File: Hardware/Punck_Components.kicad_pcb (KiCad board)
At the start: 4 copper layers, 91.2 x 99.8 mm, 112 parts, among them J1 Conn_01x12_Female, J2 Conn_01x12_Female, J3 Conn_01x12_Female, J4 Conn_01x12_Female, J5 SWD_Header, J6 Eurorack_10_pin_power, Q1 MMBT3904, Q2 MMBT3904, Q3 MMBT3904, Q4 MMBT3904, Q5 MMBT3904, Q6 MMBT3904, Q7 MMBT3904, U1 TL074, U2 STM32H743ZITx, U3 W25Q128JVS, U4 PCM5100APW, U5 TPS561201, U6 W25Q128JVS, U7 LD1117-3.3-4Tab, Y1 8MHz 20pF

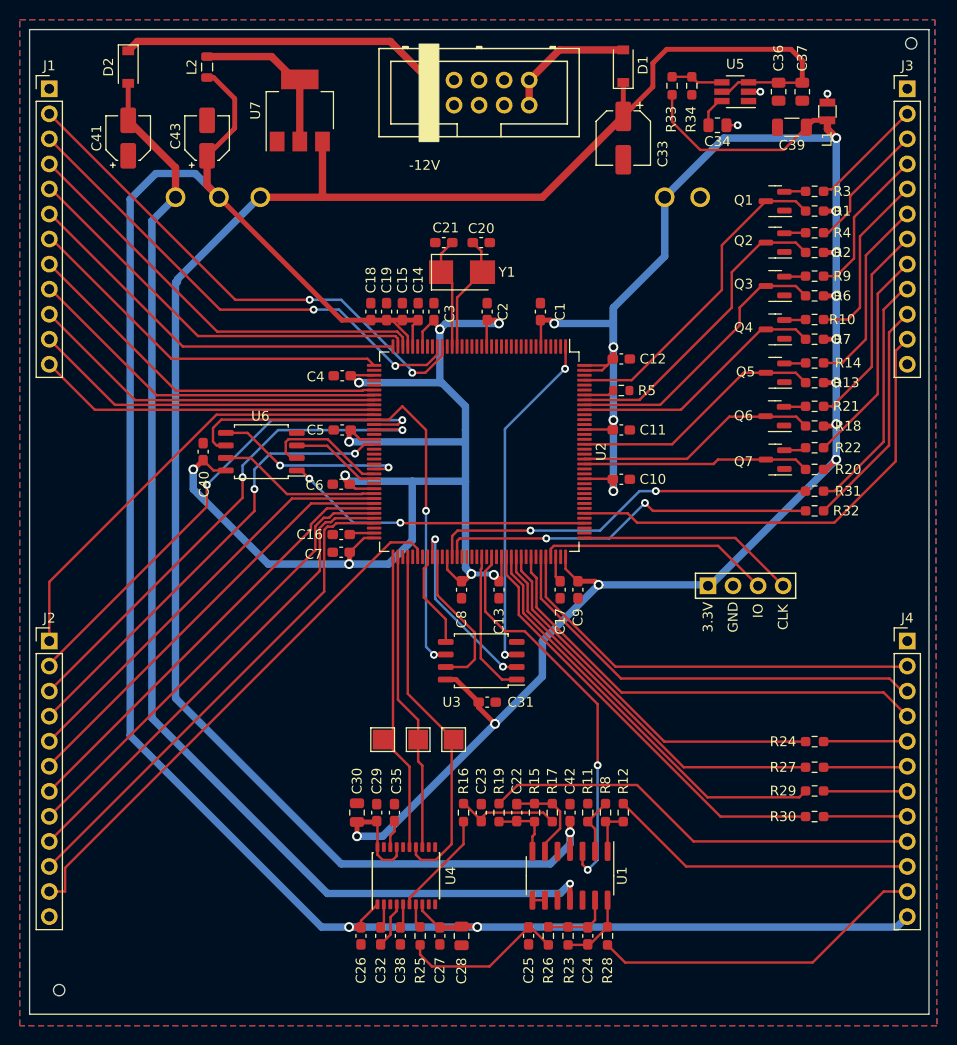
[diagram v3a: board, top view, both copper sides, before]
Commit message: Component PCB first draft
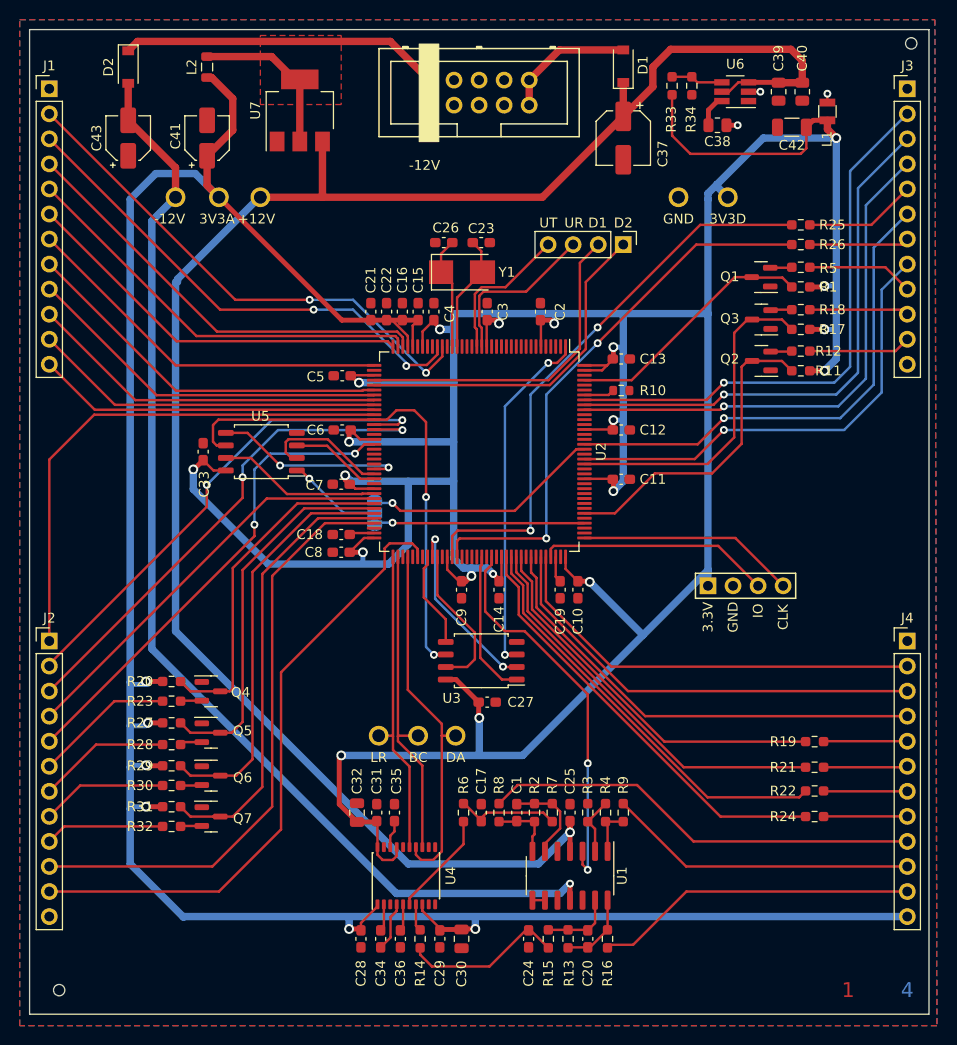
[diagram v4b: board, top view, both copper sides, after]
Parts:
- added FID1: 4_Layer_Marker, Custom_Footprints:4_Layer_Markers, F.Cu at (156.0, 147.4)
- added J5: Debug_Header, Connector_PinHeader_2.54mm:PinHeader_1x04_P2.54mm_Vertical, F.Cu at (130.2, 71.8)
- added JP1: QSPI2_NCS_Select, Jumper:SolderJumper-3_P1.3mm_Bridged12_RoundedPad1.0x1.5mm, B.Cu at (105.0, 99.0)
- C17: renamed from C23; value 1nF -> 2n2
- C24: renamed from C25; value 1nF -> 2n2
- R14: renamed from R25; value 2k2 -> 1k
- R15: renamed from R26; value 10k -> 15k
- R6: renamed from R16; value 2k2 -> 1k
- R7: renamed from R17; value 10k -> 15k
- TP1: renamed from TP6; footprint TestPoint:TestPoint_Pad_2.0x2.0mm -> Custom_Footprints:1.3mm_Test_Point
- TP2: renamed from TP7; footprint TestPoint:TestPoint_Pad_2.0x2.0mm -> Custom_Footprints:1.3mm_Test_Point
- TP3: renamed from TP8; footprint TestPoint:TestPoint_Pad_2.0x2.0mm -> Custom_Footprints:1.3mm_Test_Point
- moved R30 86.0 mm to (84.4, 126.7), turned to 0 degrees
- moved R29 83.4 mm to (84.4, 124.7), turned to 180 degrees
- moved R32 83.0 mm to (84.4, 130.8), turned to 0 degrees
- moved R31 80.6 mm to (84.4, 128.8), turned to 180 degrees
- moved Q6 78.7 mm to (88.4, 125.7), turned to 0 degrees
- moved Q7 75.6 mm to (88.4, 129.8), turned to 0 degrees
- moved R23 73.7 mm to (84.4, 118.1), turned to 0 degrees
- moved R20 71.9 mm to (84.4, 116.1), turned to 180 degrees
- moved R28 71.8 mm to (84.4, 122.5), turned to 0 degrees
- moved R27 70.1 mm to (84.4, 120.3), turned to 180 degrees
- moved Q4 65.7 mm to (88.4, 117.1), turned to 0 degrees
- moved Q5 63.6 mm to (88.4, 121.3), turned to 0 degrees
- moved R25 27.0 mm to (148.2, 69.8)
- moved R26 27.0 mm to (148.2, 71.8)
- moved Q1 14.2 mm to (144.2, 75.1)
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- renumbered C22 to C1, C9 to C10, C10 to C11, C11 to C12, C12 to C13, C13 to C14, C14 to C15, C15 to C16, C16 to C18, C17 to C19, C1 to C2, C24 to C20, C18 to C21, C19 to C22, C20 to C23, C42 to C25, C21 to C26, C31 to C27, C26 to C28, C27 to C29, C2 to C3, C28 to C30, C29 to C31, C30 to C32, C40 to C33, C32 to C34, C38 to C36, C33 to C37, C34 to C38, C36 to C39, C3 to C4, C37 to C40, C43 to C41, C39 to C42, C41 to C43, C4 to C5, C5 to C6, C6 to C7, C7 to C8, C8 to C9, J5 to J6, J6 to J7, Q6 to Q1, Q3 to Q2, Q1 to Q3, Q5 to Q4, Q7 to Q5, Q2 to Q6, Q4 to Q7, R18 to R1, R5 to R10, R6 to R11, R9 to R12, R23 to R13, R28 to R16, R1 to R17, R3 to R18, R24 to R19, R15 to R2, R13 to R20, R27 to R21, R29 to R22, R14 to R23, R30 to R24, R31 to R25, R32 to R26, R20 to R27, R22 to R28, R2 to R29, R11 to R3, R4 to R30, R7 to R31, R10 to R32, R8 to R4, R21 to R5, R19 to R8, R12 to R9, TP1 to TP4, TP2 to TP5, TP3 to TP6, TP4 to TP7, TP5 to TP8, U6 to U5, U5 to U6
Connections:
- J1 pad 10: /SAMPLER_A_VOL_POT -> /SNARE_VOL_POT
- J1 pad 11: /SAMPLER_B_VOICE_POT -> /SAMPLER_A_SPEED_POT
- J1 pad 12: /HIHAT_DECAY_POT -> /SAMPLER_B_VOICE_POT
- J1 pad 2: /SAMPLER_A_VOICE_POT -> /SNARE_FILTER_POT
- J1 pad 3: /SAMPLER_A_SPEED_POT -> /SAMPLER_A_VOICE_POT
- J1 pad 7: /SNARE_FILTER_POT -> /SNARE_TUNING_POT
- J1 pad 8: /SNARE_TUNING_POT -> /HIHAT_DECAY_POT
- J1 pad 9: /SNARE_VOL_POT -> /SAMPLER_B_SPEED_POT
- J2 pad 10: /CH_BTN -> /MIDI_LEARN
- J2 pad 11: /KI_BTN -> /SEQ_SELECT
- J2 pad 2: /SAMPLER_B_SPEED_POT -> /SAMPLER_A_VOL_POT
- J2 pad 4: /TEMPO_POT -> /CH_BTN
- J2 pad 5: /MIDI_LEARN -> /TEMPO_POT
- J2 pad 6: /SEQ_SELECT -> /CH_IN
- J2 pad 7: /SA_BTN -> /OH_IN
- J2 pad 8: /SB_BTN -> /SAMPLER_A_IN
- J2 pad 9: /SN_BTN -> /SAMPLER_B_IN
- J3 pad 10: /SB_LED -> /SNARE_IN
- J3 pad 11: /OH_BTN -> /KICK_IN
- J3 pad 12: unconnected-(J3-Pad12) -> GND
- J3 pad 2: /KICK_IN -> /SA_BTN
- J3 pad 3: /SAMPLER_A_IN -> /KI_BTN
- J3 pad 4: /SNARE_IN -> /SN_BTN
- J3 pad 5: /SAMPLER_B_IN -> /SA_LED
- J3 pad 6: /CH_IN -> /SB_BTN
- J3 pad 7: /MIDI_IN -> /SB_LED
- J3 pad 8: /OH_IN -> /OH_BTN
- J3 pad 9: /SA_LED -> /MIDI_IN
- Q1 pad 3: /MIDI_CLAMP -> /MIDI_UART
- Q2 pad 3: /SNARE_CLAMP -> /KICK_CLAMP
- Q3 pad 3: /KICK_CLAMP -> /SNARE_CLAMP
- R1 pad 1: /MIDI_CLAMP -> /MIDI_UART
- R11 pad 1: /SNARE_CLAMP -> /KICK_CLAMP
- R12 pad 1: /SNARE_IN -> /KICK_IN
- R17 pad 1: /KICK_CLAMP -> /SNARE_CLAMP
- R18 pad 1: /KICK_IN -> /SNARE_IN
- R20 pad 2: +3V3 -> +3.3VA
- R27 pad 2: +3V3 -> +3.3VA
- R29 pad 2: +3V3 -> +3.3VA
- R31 pad 2: +3V3 -> +3.3VA
- U2 pad 114: /OH_BTN -> /KICK_CLAMP
- U2 pad 124: /OH_CLAMP -> /SNARE_CLAMP
- U2 pad 125: /MIDI_CLAMP -> /OH_BTN
- U2 pad 127: unconnected-(U2-Pad127) -> /OCTOSPIM_P2_NCS
- U2 pad 128: /CH_CLAMP -> /SB_BTN
- U2 pad 135: /SAMPLER_B_CLAMP -> /SN_BTN
- U2 pad 136: /SNARE_CLAMP -> /KI_BTN
- U2 pad 137: /SAMPLER_A_CLAMP -> /SA_BTN
- U2 pad 141: /KICK_CLAMP -> /MIDI_UART
- U2 pad 18: unconnected-(U2-Pad18) -> /UART_RX
- U2 pad 19: unconnected-(U2-Pad19) -> /UART_TX
- U2 pad 26: /SAMPLER_A_VOICE_POT -> /SNARE_FILTER_POT
- U2 pad 27: /SAMPLER_A_SPEED_POT -> /SAMPLER_A_VOICE_POT
- U2 pad 37: /SNARE_FILTER_POT -> /SNARE_TUNING_POT
- U2 pad 42: /SNARE_TUNING_POT -> /HIHAT_DECAY_POT
- U2 pad 43: /SNARE_VOL_POT -> /SAMPLER_B_SPEED_POT
- U2 pad 44: /SAMPLER_A_VOL_POT -> /SNARE_VOL_POT
- U2 pad 45: /SAMPLER_B_VOICE_POT -> /SAMPLER_A_SPEED_POT
- U2 pad 46: /HIHAT_DECAY_POT -> /SAMPLER_B_VOICE_POT
- U2 pad 49: /SAMPLER_B_SPEED_POT -> /SAMPLER_A_VOL_POT
- U2 pad 64: /MIDI_LEARN -> /CH_BTN
- U2 pad 65: /SEQ_SELECT -> /CH_CLAMP
- U2 pad 66: /SA_BTN -> /OH_CLAMP
- U2 pad 67: /SB_BTN -> /SAMPLER_A_CLAMP
- U2 pad 68: /SN_BTN -> /SAMPLER_B_CLAMP
- U2 pad 69: /CH_BTN -> /MIDI_LEARN
- U2 pad 78: /KI_BTN -> /SEQ_SELECT
- U5 pad 1: /QSPI_BK2_NCS -> Net-(JP1-Pad2)
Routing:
- net /DAC2: track 0.00 -> 35.1 mm
- net /DAC1: track 0.00 -> 33.5 mm
- net /MIDI_UART: track 0.00 -> 25.8 mm
- net /MIDI_CLAMP: track 24.6 -> 0.00 mm
- net +3V3: track 373.7 -> 398.1 mm, vias 24 -> 20
- net /OCTOSPIM_P2_NCS: track 0.00 -> 24.3 mm, vias 0 -> 1
- net +3.3VA: track 210.9 -> 233.4 mm, vias 2 -> 6
- net /SAMPLER_B_CLAMP: track 26.2 -> 46.4 mm
- net /SEQ_SELECT: track 44.0 -> 63.6 mm
- net /MIDI_LEARN: track 43.1 -> 61.1 mm
- net /SA_LED_OUT: track 39.8 -> 57.7 mm
- net /SB_LED_OUT: track 38.9 -> 56.5 mm
- net /UART_RX: track 0.00 -> 16.9 mm
- net /OH_CLAMP: track 23.0 -> 38.5 mm
- net /UART_TX: track 0.00 -> 14.9 mm
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- added copper zone on F.Cu, net /VO
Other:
- board text added: "+12V"
- board text added: "-12V"
- board text added: "3V3A"
- board text added: "3V3D"
- board text added: "BC"
- board text added: "D1"
- board text added: "D2"
- board text added: "DA"
- board text added: "GND"
- board text added: "H723"
- board text added: "H743"
- board text added: "LR"
- board text added: "UR"
- board text added: "UT"

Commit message: Started panel layout
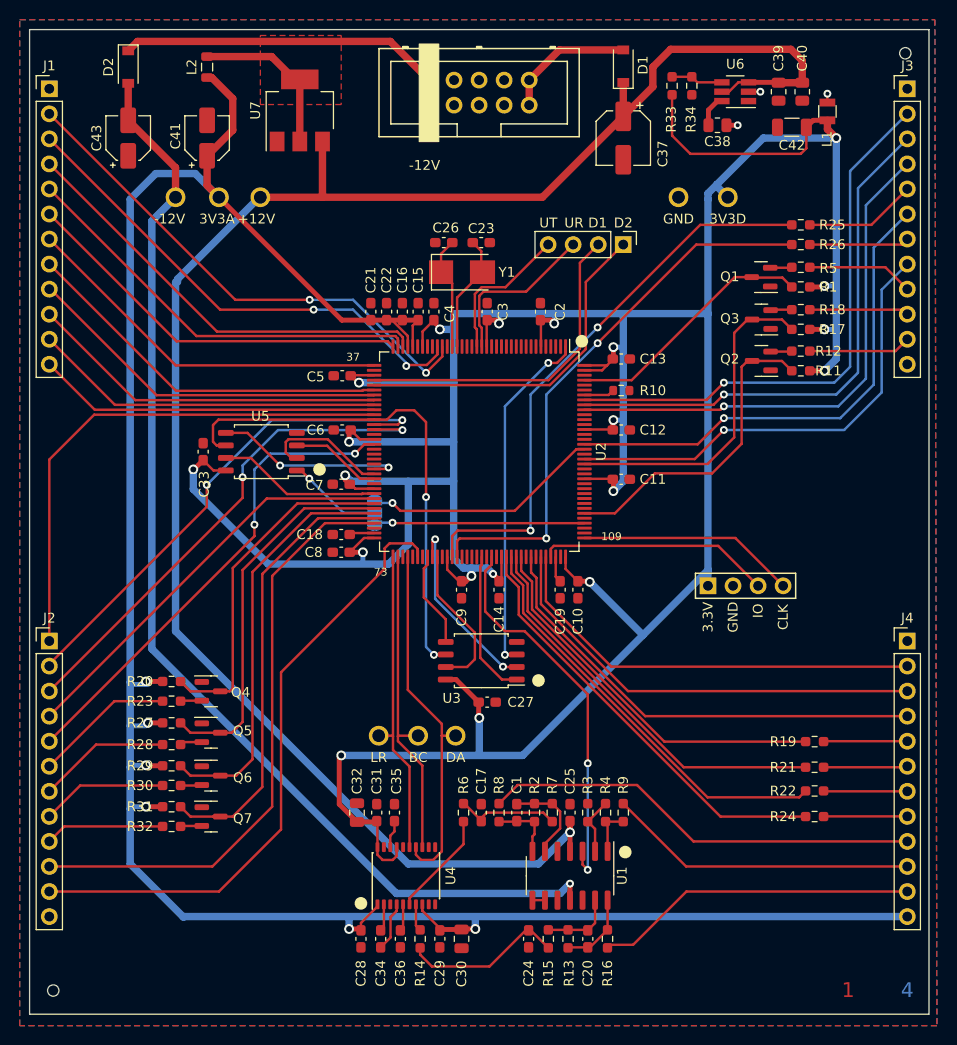
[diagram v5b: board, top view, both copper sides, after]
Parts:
- moved H2 1.17 mm to (158.8, 52.4)
- moved H1 0.60 mm to (72.4, 147.4)
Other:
- board text added: "109"
- board text added: "37"
- board text added: "73"
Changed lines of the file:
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@@
   )
   (footprint "Custom_Footprints:JLC_SMT_Tooling_Hole" (layer "F.Cu")
-    (at 73 147.4)
+    (at 72.4 147.44)
     (descr "Mounting Hole 2.2mm, no annular, M2")
     (tags "mounting hole 2.2mm no annular m2")
@@
   )
   (footprint "Custom_Footprints:JLC_SMT_Tooling_Hole" (layer "F.Cu")
-    (at 159.4 51.4)
+    (at 158.8 52.4)
     (descr "Mounting Hole 2.2mm, no annular, M2")
     (tags "mounting hole 2.2mm no annular m2")
@@
       ))
   )
+  (gr_circle (center 126 81.6) (end 126.565685 81.6) (layer "F.SilkS") (width 0.15) (fill solid))
+  (gr_circle (center 130.4 133.4) (end 130.965685 133.4) (layer "F.SilkS") (width 0.15) (fill solid))
+  (gr_circle (center 121.6 116) (end 122.165685 116) (layer "F.SilkS") (width 0.15) (fill solid))
+  (gr_circle (center 99.4 94.6) (end 99.965685 94.6) (layer "F.SilkS") (width 0.15) (fill solid))
+  (gr_circle (center 103.6 138.6) (end 104.165685 138.6) (layer "F.SilkS") (width 0.15) (fill solid))
   (gr_rect (start 93.4 52) (end 101.6 57.665779) (layer "F.Mask") (width 0.15) (fill solid))
   (gr_line locked (start 115.6 48) (end 115.6 153) (layer "Dwgs.User") (width 0.15))
@@
     (effects (font (size 1 1) (thickness 0.15)) (justify mirror))
   )
+  (gr_text "73" (at 105.6 105) (layer "F.SilkS")
+    (effects (font (size 0.8 0.8) (thickness 0.12)))
+  )
   (gr_text "DA" (at 113.2 123.8) (layer "F.SilkS")
     (effects (font (size 1 1) (thickness 0.15)))
@@
     (effects (font (size 1 1) (thickness 0.15)))
   )
+  (gr_text "37" (at 102.8 83.2) (layer "F.SilkS")
+    (effects (font (size 0.8 0.8) (thickness 0.12)))
+  )
   (gr_text "D1" (at 127.6 69.6) (layer "F.SilkS")
     (effects (font (size 1 1) (thickness 0.15)))
   )
+  (gr_text "109" (at 129 101.4) (layer "F.SilkS")
+    (effects (font (size 0.8 0.8) (thickness 0.12)))
+  )
   (gr_text "UT" (at 122.6 69.6) (layer "F.SilkS")

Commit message: Updated components on panel board
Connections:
- J1 pad 12: /SAMPLER_B_VOICE_POT -> /SAMPLER_B_SPEED_POT
- J1 pad 9: /SAMPLER_B_SPEED_POT -> /SAMPLER_B_VOICE_POT
- U2 pad 43: /SAMPLER_B_SPEED_POT -> /SAMPLER_B_VOICE_POT
- U2 pad 46: /SAMPLER_B_VOICE_POT -> /SAMPLER_B_SPEED_POT
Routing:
- net /SAMPLER_B_VOICE_POT: track 34.8 -> 37.4 mm
- net /SAMPLER_B_SPEED_POT: track 37.4 -> 34.8 mm
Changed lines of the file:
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@@
       (net 25 "/HIHAT_DECAY_POT") (pinfunction "Pin_8") (pintype "passive"))
     (pad "9" thru_hole oval (at 0 20.32) (size 1.7 1.7) (drill 1) (layers *.Cu *.Mask)
-      (net 31 "/SAMPLER_B_SPEED_POT") (pinfunction "Pin_9") (pintype "passive"))
+      (net 30 "/SAMPLER_B_VOICE_POT") (pinfunction "Pin_9") (pintype "passive"))
     (pad "10" thru_hole oval (at 0 22.86) (size 1.7 1.7) (drill 1) (layers *.Cu *.Mask)
       (net 23 "/SNARE_VOL_POT") (pinfunction "Pin_10") (pintype "passive"))
@@
       (net 28 "/SAMPLER_A_SPEED_POT") (pinfunction "Pin_11") (pintype "passive"))
     (pad "12" thru_hole oval (at 0 27.94) (size 1.7 1.7) (drill 1) (layers *.Cu *.Mask)
-      (net 30 "/SAMPLER_B_VOICE_POT") (pinfunction "Pin_12") (pintype "passive"))
+      (net 31 "/SAMPLER_B_SPEED_POT") (pinfunction "Pin_12") (pintype "passive"))
     (model "${KICAD6_3DMODEL_DIR}/Connector_PinHeader_2.54mm.3dshapes/PinHeader_1x12_P2.54mm_Vertical.wrl"
       (offset (xyz 0 0 0))
@@
       (net 25 "/HIHAT_DECAY_POT") (pinfunction "PA6") (pintype "bidirectional"))
     (pad "43" smd roundrect (at -5.75 10.6625 270) (size 0.3 1.475) (layers "F.Cu" "F.Paste" "F.Mask") (roundrect_rratio 0.25)
-      (net 31 "/SAMPLER_B_SPEED_POT") (pinfunction "PA7") (pintype "bidirectional"))
+      (net 30 "/SAMPLER_B_VOICE_POT") (pinfunction "PA7") (pintype "bidirectional"))
     (pad "44" smd roundrect (at -5.25 10.6625 270) (size 0.3 1.475) (layers "F.Cu" "F.Paste" "F.Mask") (roundrect_rratio 0.25)
       (net 23 "/SNARE_VOL_POT") (pinfunction "PC4") (pintype "bidirectional"))
@@
       (net 28 "/SAMPLER_A_SPEED_POT") (pinfunction "PC5") (pintype "bidirectional"))
     (pad "46" smd roundrect (at -4.25 10.6625 270) (size 0.3 1.475) (layers "F.Cu" "F.Paste" "F.Mask") (roundrect_rratio 0.25)
-      (net 30 "/SAMPLER_B_VOICE_POT") (pinfunction "PB0") (pintype "bidirectional"))
+      (net 31 "/SAMPLER_B_SPEED_POT") (pinfunction "PB0") (pintype "bidirectional"))
     (pad "47" smd roundrect (at -3.75 10.6625 270) (size 0.3 1.475) (layers "F.Cu" "F.Paste" "F.Mask") (roundrect_rratio 0.25)
       (net 26 "/HIHAT_VOL_POT") (pinfunction "PB1") (pintype "bidirectional"))
@@
   (segment (start 107.8 89.6) (end 94.54 89.6) (width 0.25) (layer "B.Cu") (net 29))
   (segment (start 94.54 89.6) (end 87.97 96.17) (width 0.25) (layer "B.Cu") (net 29))
-  (segment (start 76.61 88.55) (end 104.9375 88.55) (width 0.25) (layer "F.Cu") (net 30))
-  (segment (start 72 83.94) (end 76.61 88.55) (width 0.25) (layer "F.Cu") (net 30))
-  (segment (start 104.913488 87.074012) (end 104.9375 87.05) (width 0.25) (layer "F.Cu") (net 31))
-  (segment (start 72.12 76.32) (end 82.874012 87.074012) (width 0.25) (layer "F.Cu") (net 31))
-  (segment (start 82.874012 87.074012) (end 104.913488 87.074012) (width 0.25) (layer "F.Cu") (net 31))
-  (segment (start 72 76.32) (end 72.12 76.32) (width 0.25) (layer "F.Cu") (net 31))
+  (segment (start 104.913488 87.074012) (end 104.9375 87.05) (width 0.25) (layer "F.Cu") (net 30))
+  (segment (start 72.12 76.32) (end 82.874012 87.074012) (width 0.25) (layer "F.Cu") (net 30))
+  (segment (start 82.874012 87.074012) (end 104.913488 87.074012) (width 0.25) (layer "F.Cu") (net 30))
+  (segment (start 72 76.32) (end 72.12 76.32) (width 0.25) (layer "F.Cu") (net 30))
+  (segment (start 76.61 88.55) (end 104.9375 88.55) (width 0.25) (layer "F.Cu") (net 31))
+  (segment (start 72 83.94) (end 76.61 88.55) (width 0.25) (layer "F.Cu") (net 31))
   (segment (start 104.9375 90.55) (end 107.748501 90.55) (width 0.25) (layer "F.Cu") (net 32))
   (segment (start 91.6 97.48) (end 91.6 95.4) (width 0.25) (layer "F.Cu") (net 32))
@@
   (via (at 150.6 80.4) (size 1) (drill 0.6) (layers "F.Cu" "B.Cu") (net 45))
   (via (at 117 105.2) (size 0.8) (drill 0.4) (layers "F.Cu" "B.Cu") (net 45))
+  (segment (start 139.7 65.9) (end 139.7 65.7) (width 0.75) (layer "B.Cu") (net 45))
   (segment (start 94.2 104.2) (end 86.6 96.6) (width 0.75) (layer "B.Cu") (net 45))
   (segment (start 116.4 104.6) (end 117 105.2) (width 0.75) (layer "B.Cu") (net 45))
-  (segment (start 140.8 67) (end 139.7 65.9) (width 0.75) (layer "B.Cu") (net 45))
   (segment (start 151.8 76.2) (end 151.8 80.6) (width 0.75) (layer "B.Cu") (net 45))
   (segment (start 86.6 96.6) (end 86.6 94.6) (width 0.75) (layer "B.Cu") (net 45))
@@
   (segment (start 130 82.2) (end 130.2 82.4) (width 0.5) (layer "B.Cu") (net 45))
   (segment (start 139.7 65.7) (end 144.4 61) (width 0.75) (layer "B.Cu") (net 45))
-  (segment (start 139.7 65.9) (end 139.7 65.7) (width 0.75) (layer "B.Cu") (net 45))
   (segment (start 114.8 104.6) (end 114.8 105.4) (width 0.75) (layer "B.Cu") (net 45))
   (segment (start 151.8 83.4) (end 150.6 84.6) (width 0.75) (layer "B.Cu") (net 45))
@@
   (segment (start 113 85.8) (end 113 80.6) (width 0.75) (layer "B.Cu") (net 45))
   (segment (start 150.6 76) (end 151.6 76) (width 0.5) (layer "B.Cu") (net 45))
-  (segment (start 140.79 67.21) (end 140.8 67.2) (width 0.75) (layer "B.Cu") (net 45))
   (segment (start 113 79) (end 113.2 78.8) (width 0.75) (layer "B.Cu") (net 45))
   (segment (start 151.6 76) (end 151.8 76.2) (width 0.5) (layer "B.Cu") (net 45))
   (segment (start 130.2 89.6) (end 130.2 95.8) (width 0.75) (layer "B.Cu") (net 45))
   (segment (start 151.8 61) (end 151.8 76.2) (width 0.75) (layer "B.Cu") (net 45))
+  (segment (start 140.8 67) (end 139.7 65.9) (width 0.75) (layer "B.Cu") (net 45))
   (segment (start 138.8 78.8) (end 123.2 78.8) (width 0.75) (layer "B.Cu") (net 45))
   (segment (start 117.6 79.8) (end 117.6 78.8) (width 0.5) (layer "B.Cu") (net 45))
@@
     )
   )
-  (zone (net 0) (net_name "") (layer "F.Cu") (hatch edge 0.508)
-    (connect_pads (clearance 0))
-    (min_thickness 0.254)
-    (keepout (tracks allowed) (vias allowed) (pads allowed ) (copperpour not_allowed) (footprints allowed))
-    (fill (thermal_gap 0.508) (thermal_bridge_width 0.508))
-    (polygon
-      (pts
-        (xy 102.2 57.8)
-        (xy 102.2 58.2)
-        (xy 92.8 58.2)
-        (xy 92.8 57.8)
-      )
-    )
-  )
-  (zone (net 0) (net_name "") (layer "F.Cu") (hatch edge 0.508)
-    (connect_pads (clearance 0))
-    (min_thickness 0.254)
-    (keepout (tracks allowed) (vias allowed) (pads allowed ) (copperpour not_allowed) (footprints allowed))
-    (fill (thermal_gap 0.508) (thermal_bridge_width 0.508))
-    (polygon
-      (pts
-        (xy 102.2 57.8)
-        (xy 101.8 57.8)
-        (xy 101.8 50.6)
-        (xy 102.2 50.6)
-      )
-    )
-  )
-  (zone (net 0) (net_name "") (layer "F.Cu") (hatch edge 0.508)
-    (connect_pads (clearance 0))
-    (min_thickness 0.254)
-    (keepout (tracks allowed) (vias allowed) (pads allowed ) (copperpour not_allowed) (footprints allowed))
-    (fill (thermal_gap 0.508) (thermal_bridge_width 0.508))
-    (polygon
-      (pts
-        (xy 93.2 57.8)
-        (xy 92.8 57.8)
-        (xy 92.8 50.6)
-        (xy 93.2 50.6)
-      )
-    )
-  )
   (zone (net 143) (net_name "/VO") (layer "F.Cu") (hatch edge 0.508)
+    (priority 1)
     (connect_pads yes (clearance 0.508))
     (min_thickness 0.254) (filled_areas_thickness no)

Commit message: Rough panel layout
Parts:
- added RESET1: SW_Push, Custom_Footprints:SW_SPST_EVQQ2, F.Cu at (99.8, 70.8)
- J1, J2, J3, J4: moved to B.Cu
- turned J1 to 180 degrees
- turned J2 to 180 degrees
- turned J3 to 180 degrees
- turned J4 to 180 degrees
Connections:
- U2 pad 25: /RESET -> Net-(U2-Pad25)
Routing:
- net Net-(U2-Pad25): track 0.00 -> 22.7 mm
- net +3.3VA: track 233.4 -> 234.3 mm
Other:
- board text added: "Reset"
